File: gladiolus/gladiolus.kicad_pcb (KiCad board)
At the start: 2 copper layers, 70.7 x 53.3 mm, 146 parts, among them J1 NEIGHBOR1, J2 NEIGHBOR2, J7 BONUS_ROW, Q1 Q_NPN_BEC, U1 THS4520RGT, U2 AD8330ARQZ, U3 AD9283, U4 AD9704, U5 LMH6643, U6 74LVC1G3157, U7 74LVC1G3157, U8 AT34C02D

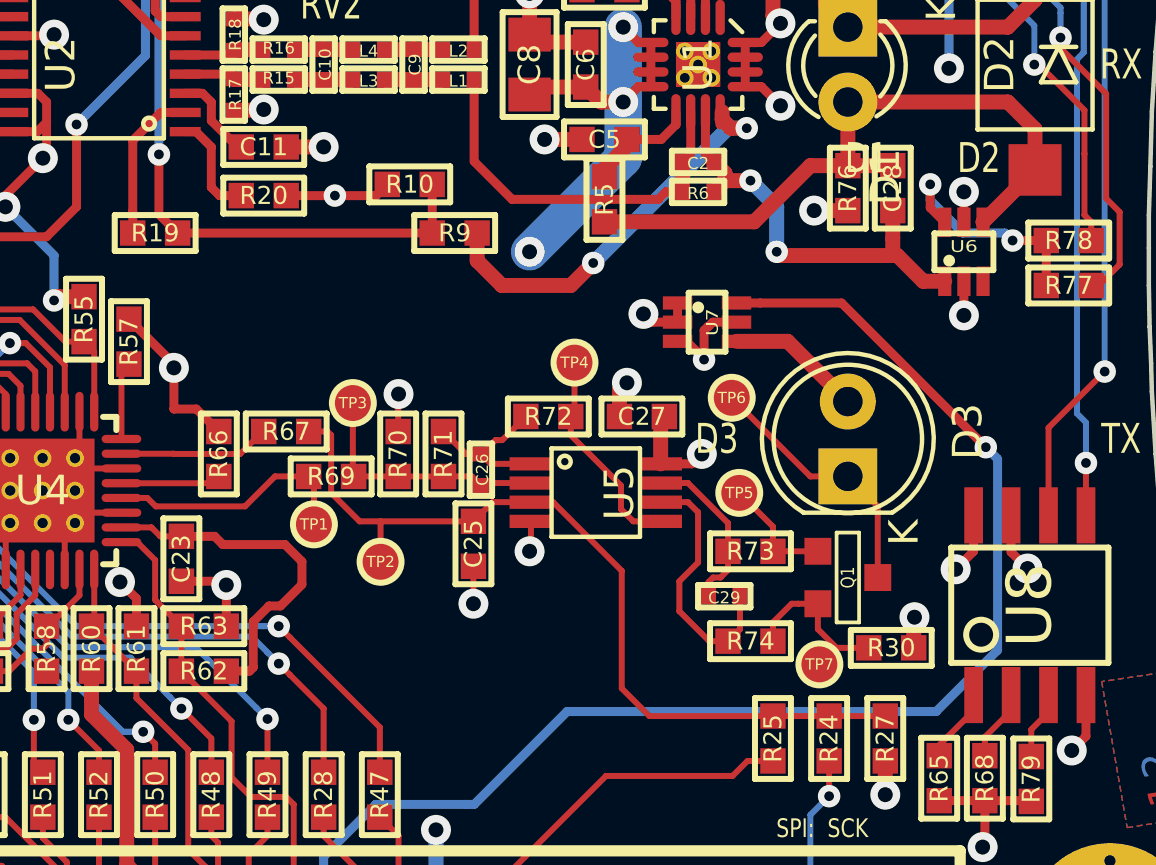
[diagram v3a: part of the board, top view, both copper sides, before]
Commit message: Added design notes for test points, EEPROM
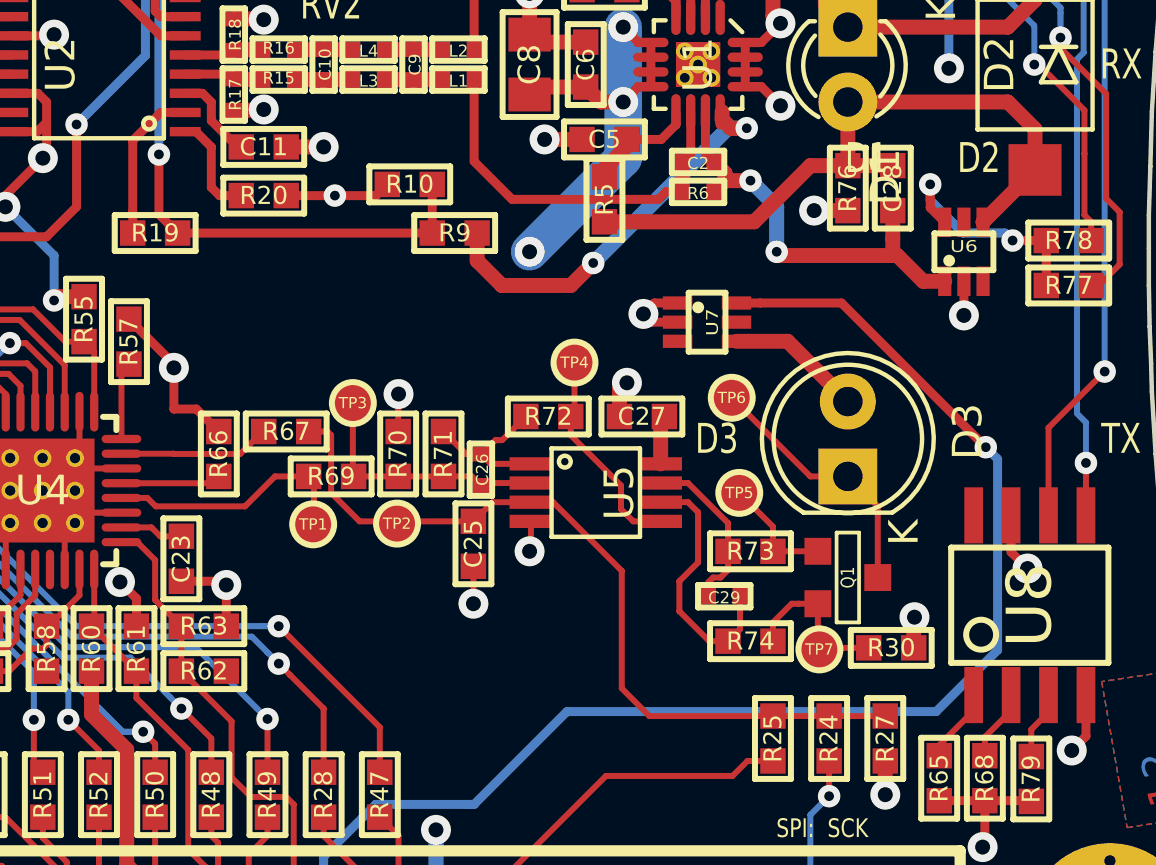
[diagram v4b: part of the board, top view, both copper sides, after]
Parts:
- moved TP2 1.41 mm to (152.3, 104.5)
- moved TP7 0.51 mm to (166.7, 108.7)
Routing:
- net VCC: track 142.4 -> 124.4 mm, vias 18 -> 14
- net Net-(C25-Pad1): track 28.9 -> 27.6 mm
- net GND: track 92.4 -> 93.0 mm
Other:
- rule pad_to_mask_clearance: 0.127 -> 0.08
- rule solder_mask_min_width: 0.25 -> 0.01
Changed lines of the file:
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@@
     (thickness 1.6)
     (drawings 129)
-    (tracks 1092)
+    (tracks 1064)
     (zones 0)
     (modules 146)
@@
     (pad_size 1.524 1.524)
     (pad_drill 0.762)
-    (pad_to_mask_clearance 0.127)
-    (solder_mask_min_width 0.25)
+    (pad_to_mask_clearance 0.08)
+    (solder_mask_min_width 0.01)
     (pad_to_paste_clearance_ratio -0.05)
     (aux_axis_origin 0 0)
@@
   )
   (module gsg-modules:TESTPOINT-50MIL (layer F.Cu)
-    (at 149.5298 104.4956)
+    (at 149.5044 104.4956)
     (fp_text reference TP1 (at 0 0) (layer F.SilkS)
       (effects (font (size 0.381 0.381) (thickness 0.09652)))
@@
   )
   (module gsg-modules:TESTPOINT-50MIL (layer F.Cu)
-    (at 151.7904 105.7656)
+    (at 152.3492 104.4702)
     (fp_text reference TP2 (at 0 0) (layer F.SilkS)
       (effects (font (size 0.381 0.381) (thickness 0.09652)))
@@
   )
   (module gsg-modules:TESTPOINT-50MIL (layer F.Cu)
-    (at 166.6748 109.2454)
+    (at 166.6748 108.7374)
     (fp_text reference TP7 (at 0 0) (layer F.SilkS)
       (effects (font (size 0.381 0.381) (thickness 0.09652)))
@@
   (segment (start 159.893 100.838) (end 159.893 99.949) (width 0.508) (layer F.Cu) (net 1) (status 10))
   (segment (start 159.893 99.949) (end 160.147 99.695) (width 0.508) (layer F.Cu) (net 1))
-  (via (at 160.7058 97.3582) (size 1.016) (drill 0.508) (layers F.Cu B.Cu) (net 1))
-  (segment (start 161.8648 97.6376) (end 161.8648 96.9876) (width 0.3048) (layer F.Cu) (net 1) (status 30))
-  (segment (start 160.9852 97.6376) (end 160.7058 97.3582) (width 0.3048) (layer F.Cu) (net 1))
-  (segment (start 161.8648 97.6376) (end 160.9852 97.6376) (width 0.3048) (layer F.Cu) (net 1) (status 10))
   (segment (start 167.64 76.2) (end 167.64 76.9874) (width 0.3048) (layer F.Cu) (net 1) (status 10))
   (segment (start 167.64 76.9874) (end 166.7256 77.9018) (width 0.3048) (layer F.Cu) (net 1))
@@
   (segment (start 168.402 85.725) (end 169.3164 85.725) (width 0.508) (layer F.Cu) (net 1))
   (segment (start 169.3164 85.725) (end 169.5704 85.979) (width 0.508) (layer F.Cu) (net 1))
+  (segment (start 161.0764 96.9876) (end 160.7058 97.3582) (width 0.3048) (layer F.Cu) (net 1))
+  (via (at 160.7058 97.3582) (size 1.016) (drill 0.508) (layers F.Cu B.Cu) (net 1))
+  (segment (start 161.8648 97.6376) (end 160.9852 97.6376) (width 0.3048) (layer F.Cu) (net 1) (status 10))
+  (segment (start 160.9852 97.6376) (end 160.7058 97.3582) (width 0.3048) (layer F.Cu) (net 1))
+  (segment (start 161.8648 96.9876) (end 161.0764 96.9876) (width 0.3048) (layer F.Cu) (net 1))
   (segment (start 142.494 82.55) (end 146.558 78.486) (width 1.27) (layer B.Cu) (net 2))
   (segment (start 146.558 78.486) (end 147.828 78.486) (width 1.27) (layer B.Cu) (net 2))
@@
   (segment (start 153.67 117.299234) (end 153.67 114.8588) (width 0.508) (layer B.Cu) (net 2))
   (via (at 153.67 114.8588) (size 1.016) (drill 0.508) (layers F.Cu B.Cu) (net 2))
-  (segment (start 147.4724 109.347) (end 147.3454 109.474) (width 0.3048) (layer F.Cu) (net 2))
-  (segment (start 147.3454 109.474) (end 146.558 109.474) (width 0.3048) (layer F.Cu) (net 2) (status 20))
-  (segment (start 147.4724 107.798614) (end 147.4724 109.347) (width 0.3048) (layer F.Cu) (net 2))
-  (segment (start 145.034 104.902) (end 146.161758 104.902) (width 0.3048) (layer F.Cu) (net 2) (status 10))
-  (segment (start 149.123401 106.536745) (end 148.395947 107.264199) (width 0.3048) (layer F.Cu) (net 2))
-  (segment (start 146.161758 104.902) (end 146.441157 105.181399) (width 0.3048) (layer F.Cu) (net 2))
-  (segment (start 146.441157 105.181399) (end 148.548345 105.181399) (width 0.3048) (layer F.Cu) (net 2))
-  (segment (start 148.548345 105.181399) (end 149.123401 105.756455) (width 0.3048) (layer F.Cu) (net 2))
-  (segment (start 149.123401 105.756455) (end 149.123401 106.536745) (width 0.3048) (layer F.Cu) (net 2))
-  (segment (start 148.395947 107.264199) (end 148.006815 107.264199) (width 0.3048) (layer F.Cu) (net 2))
-  (segment (start 148.006815 107.264199) (end 147.4724 107.798614) (width 0.3048) (layer F.Cu) (net 2))
   (segment (start 143.1798 116.050566) (end 143.1798 112.137954) (width 0.508) (layer F.Cu) (net 2))
   (segment (start 141.986 110.4138) (end 141.986 109.474) (width 0.508) (layer F.Cu) (net 2) (status 20))
@@
   (via (at 139.7 82.55) (size 1.016) (drill 0.508) (layers F.Cu B.Cu) (net 2))
   (segment (start 139.7 82.55) (end 142.494 82.55) (width 1.27) (layer B.Cu) (net 2))
-  (via (at 162.687 102.108) (size 1.016) (drill 0.508) (layers F.Cu B.Cu) (net 2))
-  (segment (start 161.29 102.444) (end 162.351 102.444) (width 0.3048) (layer F.Cu) (net 2) (status 10))
-  (segment (start 162.351 102.444) (end 162.687 102.108) (width 0.3048) (layer F.Cu) (net 2))
-  (via (at 171.577 93.218) (size 1.016) (drill 0.508) (layers F.Cu B.Cu) (net 2))
-  (segment (start 171.577 94.25) (end 171.577 93.218) (width 0.3048) (layer F.Cu) (net 2) (status 10))
   (via (at 140.716 96.901) (size 0.762) (drill 0.3302) (layers F.Cu B.Cu) (net 2))
   (segment (start 141.732 96.774) (end 140.843 96.774) (width 0.508) (layer F.Cu) (net 2) (status 10))
@@
   (segment (start 161.29 100.965) (end 161.417 100.838) (width 0.508) (layer F.Cu) (net 2) (status 30))
   (segment (start 161.29 102.444) (end 161.29 100.965) (width 0.508) (layer F.Cu) (net 2) (status 30))
-  (segment (start 161.8648 98.2876) (end 162.1686 98.2876) (width 0.3048) (layer F.Cu) (net 2) (status 30))
-  (via (at 162.7632 98.9076) (size 0.762) (drill 0.3302) (layers F.Cu B.Cu) (net 2))
-  (segment (start 162.1686 98.2876) (end 162.7632 98.8822) (width 0.3048) (layer F.Cu) (net 2) (status 10))
-  (segment (start 162.7632 98.8822) (end 162.7632 98.9076) (width 0.3048) (layer F.Cu) (net 2))
-  (segment (start 163.06 97.6376) (end 162.9156 97.782) (width 0.3048) (layer F.Cu) (net 2))
-  (segment (start 163.8648 97.6376) (end 163.06 97.6376) (width 0.3048) (layer F.Cu) (net 2) (status 10))
-  (segment (start 162.9156 97.782) (end 162.8982 97.782) (width 0.3048) (layer F.Cu) (net 2))
-  (segment (start 162.7632 97.917) (end 162.7632 98.9076) (width 0.3048) (layer F.Cu) (net 2))
-  (segment (start 162.8982 97.782) (end 162.7632 97.917) (width 0.3048) (layer F.Cu) (net 2))
   (segment (start 173.8376 113.8682) (end 173.863 113.8936) (width 0.3048) (layer F.Cu) (net 2))
   (segment (start 170.7388 113.8682) (end 173.8376 113.8682) (width 0.3048) (layer F.Cu) (net 2))
@@
   (segment (start 172.2882 113.8682) (end 172.2882 115.3668) (width 0.3048) (layer F.Cu) (net 2))
   (segment (start 172.2882 115.3668) (end 172.212 115.443) (width 0.3048) (layer F.Cu) (net 2))
-  (via (at 171.2976 106.0196) (size 1.016) (drill 0.508) (layers F.Cu B.Cu) (net 2))
-  (segment (start 171.9072 104.1908) (end 171.9072 105.41) (width 0.3048) (layer F.Cu) (net 2))
-  (segment (start 171.9072 105.41) (end 171.2976 106.0196) (width 0.3048) (layer F.Cu) (net 2))
   (segment (start 121.92 71.12) (end 123.088401 69.951599) (width 0.508) (layer F.Cu) (net 3) (status 10))
   (segment (start 123.088401 69.951599) (end 170.740833 69.951599) (width 0.508) (layer F.Cu) (net 3))
@@
   (segment (start 159.971602 110.060602) (end 160.909 110.998) (width 0.2032) (layer F.Cu) (net 75))
   (segment (start 151.7904 104.394) (end 154.305 104.394) (width 0.2032) (layer F.Cu) (net 75))
-  (segment (start 151.7904 104.394) (end 151.7904 105.7656) (width 0.2032) (layer F.Cu) (net 75) (status 20))
   (segment (start 151.079198 104.394) (end 151.7904 104.394) (width 0.2032) (layer F.Cu) (net 75))
   (segment (start 155.9179 101.6381) (end 156.718 100.838) (width 0.2032) (layer F.Cu) (net 76) (status 20))

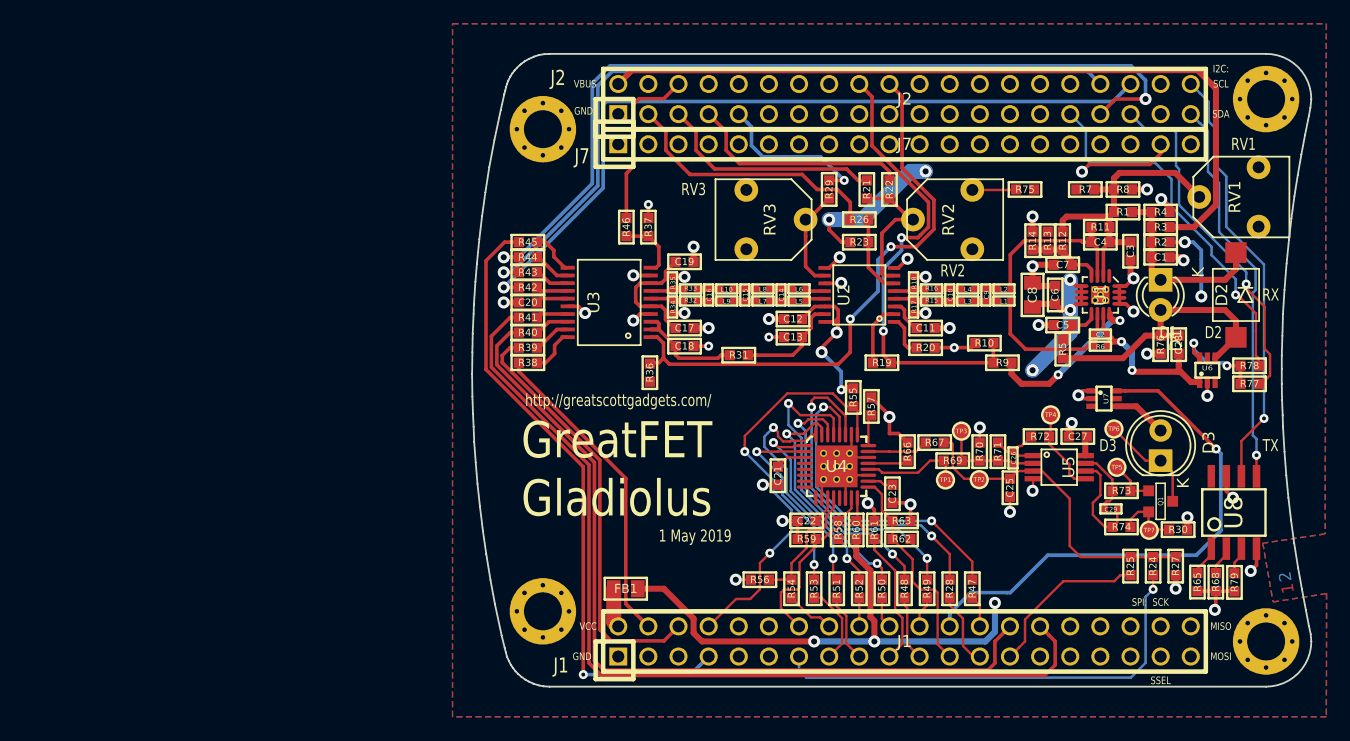
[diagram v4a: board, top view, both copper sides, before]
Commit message: Added test points, changed EEPROM package and connections.
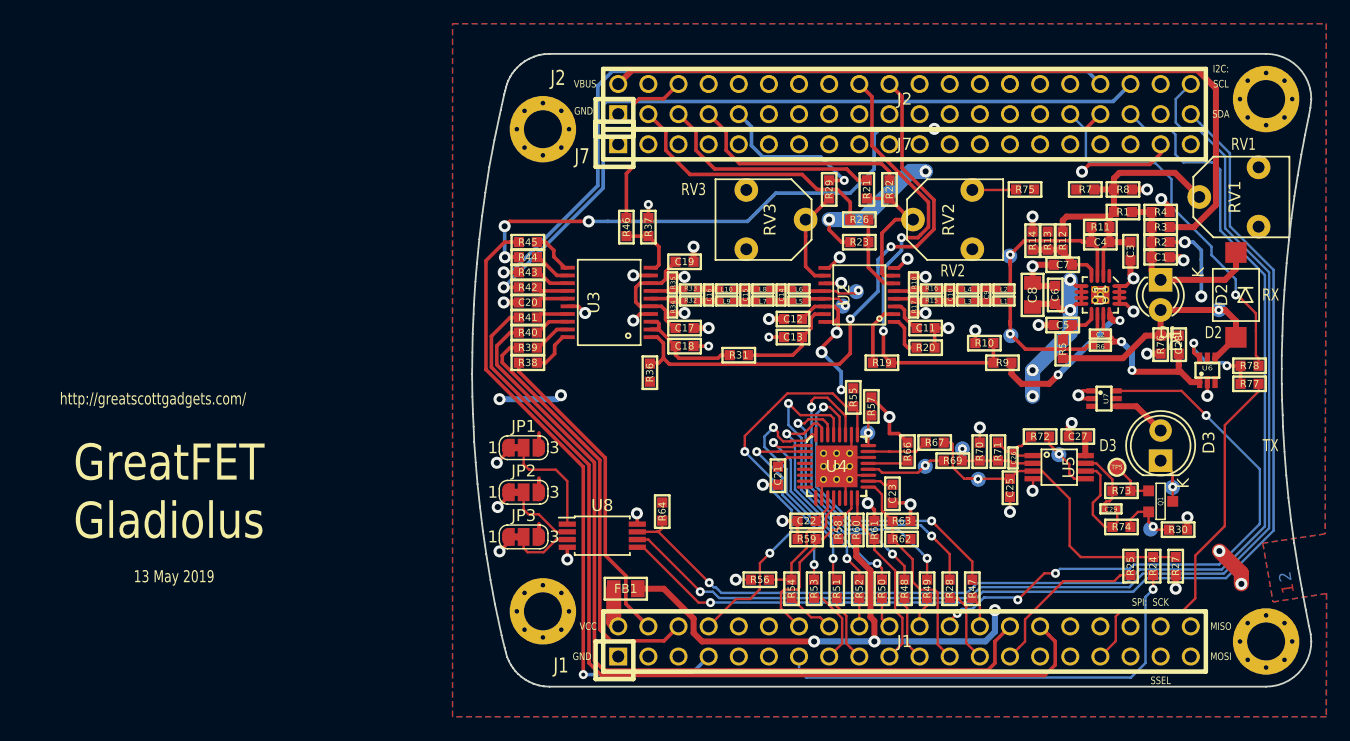
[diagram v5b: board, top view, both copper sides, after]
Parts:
- removed R65, R68, R79: 1k, gsg-modules:0603
- added JP1: Jumper_3_Bridged12, Jumper:SolderJumper-3_P1.3mm_Bridged12_RoundedPad1.0x1.5mm_NumberLabels, F.Cu at (113.9, 101.8)
- added JP2: Jumper_3_Bridged12, Jumper:SolderJumper-3_P1.3mm_Bridged12_RoundedPad1.0x1.5mm_NumberLabels, F.Cu at (113.9, 105.5)
- added JP3: Jumper_3_Bridged12, Jumper:SolderJumper-3_P1.3mm_Bridged12_RoundedPad1.0x1.5mm_NumberLabels, F.Cu at (113.9, 109.3)
- added R64: 10k, gsg-modules:0603, F.Cu at (125.6, 107.2)
- added TP10: TestPoint, gsg-modules:TESTPOINT-50MIL, B.Cu at (155.0, 92.3)
- added TP11: TestPoint, gsg-modules:TESTPOINT-50MIL, B.Cu at (154.9, 85.6)
- added TP12: TestPoint, gsg-modules:TESTPOINT-50MIL, B.Cu at (140.8, 89.8)
- added TP13: TestPoint, gsg-modules:TESTPOINT-50MIL, B.Cu at (142.0, 88.6)
- added TP8: TestPoint, gsg-modules:TESTPOINT-50MIL, B.Cu at (172.5, 90.1)
- added TP9: TestPoint, gsg-modules:TESTPOINT-50MIL, B.Cu at (143.0, 100.5)
- TP1, TP2, TP3, TP4, TP6, TP7: moved to B.Cu
- U8: footprint gsg-modules:SOIC8-154 -> Package_SO:TSSOP-8_4.4x3mm_P0.65mm
- moved U8 53.3 mm to (120.6, 109.2), turned to 0 degrees
- moved TP6 6.97 mm to (168.6, 105.1)
- moved TP4 3.42 mm to (159.1, 102.4)
- moved TP1 2.05 mm to (147.8, 103.4)
- moved TP3 1.50 mm to (150.9, 101.9)
- moved TP7 0.16 mm to (166.8, 108.6)
- moved TP2 0.08 mm to (152.3, 104.4)
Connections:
- J1 pad 33: (no net) -> /P9_5
- R77 pad 2: /P2_1 -> /P9_5
- U8 pad 7: GND -> /P2_1
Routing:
- net /P2_1: track 29.5 -> 100.7 mm
- net /I2C0_SCL: track 36.4 -> 99.8 mm
- net /I2C0_SDA: track 33.0 -> 96.1 mm
- net /P9_5: track 0.00 -> 31.5 mm
- net /P2_2: track 73.4 -> 61.0 mm, vias 2 -> 4
- net Net-(JP1-Pad2): track 3.05 -> 9.29 mm
- net VCC: track 124.4 -> 130.2 mm, vias 14 -> 17
- net /P5_4: track 44.4 -> 49.6 mm, vias 1 -> 4
- net /TXOUT: track 8.89 -> 4.59 mm, vias 0 -> 1
- net GND: track 93.0 -> 97.3 mm, vias 45 -> 49
- net Net-(JP2-Pad2): track 2.54 -> 5.91 mm
- net Net-(L6-Pad2): track 1.70 -> 4.73 mm, vias 0 -> 1
- net Net-(JP3-Pad2): track 2.32 -> 5.22 mm
- net Net-(L5-Pad2): track 1.70 -> 3.69 mm, vias 0 -> 1
- net Net-(C26-Pad1): track 8.83 -> 7.34 mm, vias 0 -> 1
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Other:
- board text added: "13 May 2019"
- board text added: "mount TX diode on reverse side"
- board text removed: "1 May 2019"
- board text removed: "mount either RX or TX diode on reverse side"
